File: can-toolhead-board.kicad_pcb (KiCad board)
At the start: 4 copper layers, 51 x 36.9 mm, 100 parts, among them J1 MF3-2x2P, J10 PH-2P, J11 PH-2P, J12 PH-2P, J13 PH-2P, J14 PH-2P, J15 PH-3P, J2 USB_C_Receptacle_USB2.0, J3 SH-6P, J4 PH-2P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

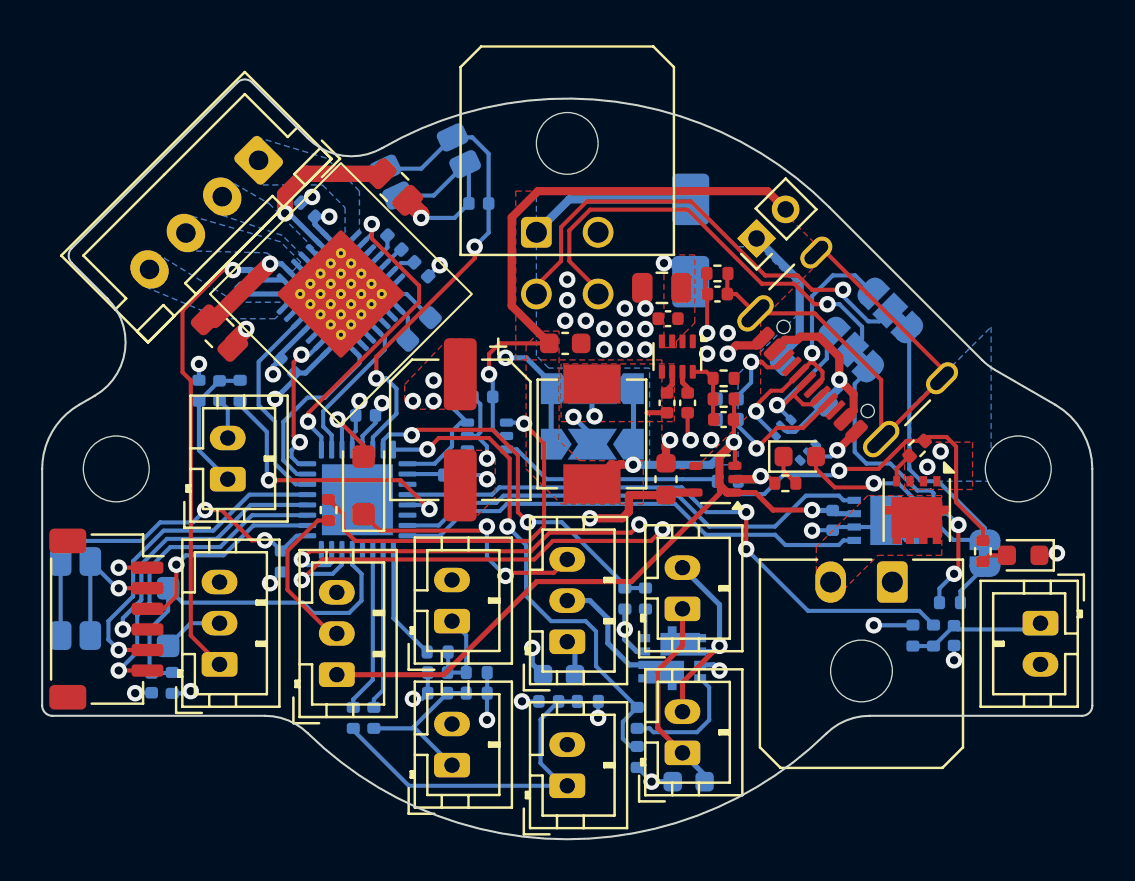
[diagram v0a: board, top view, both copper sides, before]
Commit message: Fixed up QFN pad routing and bypass cap vias
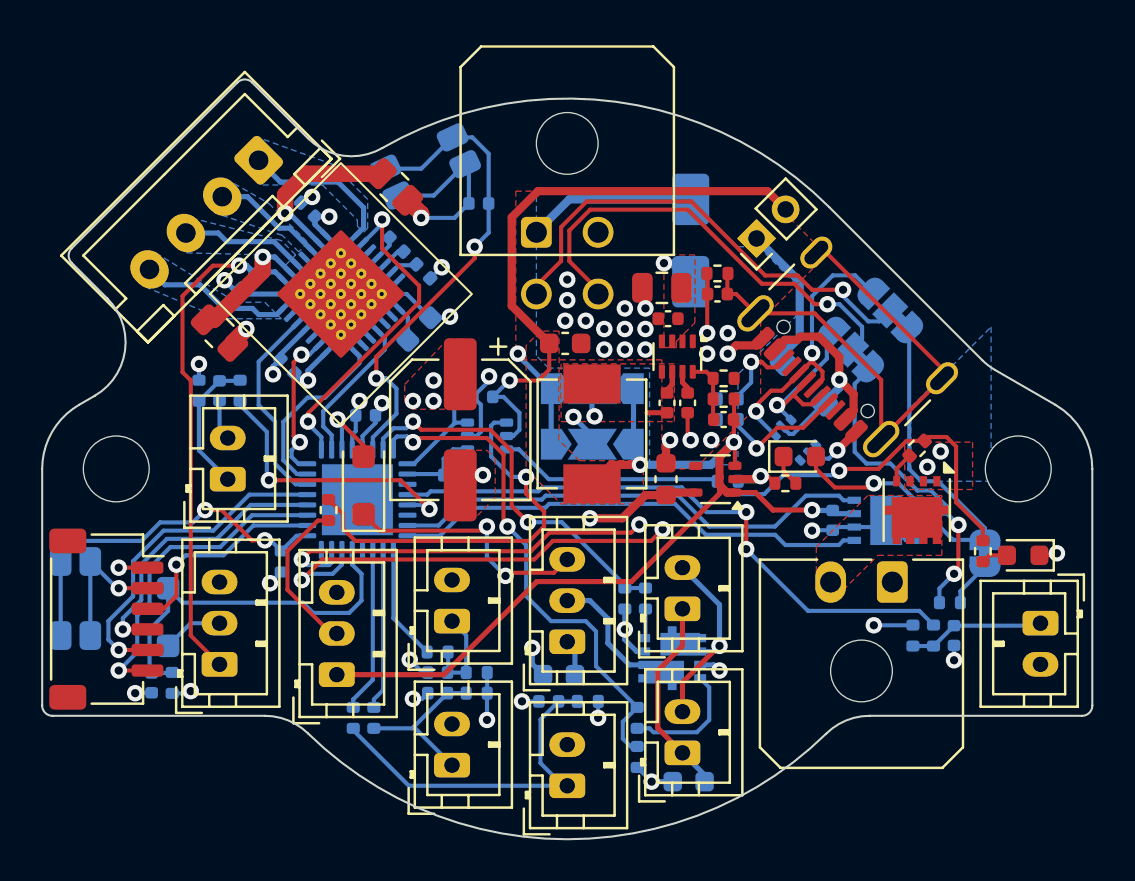
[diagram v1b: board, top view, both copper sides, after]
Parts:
- moved C16 0.14 mm to (93.0, 90.4)
- moved C17 0.14 mm to (91.7, 89.1)
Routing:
- net Net-(J9-Pin_1): track 0.00 -> 7.62 mm
- net Net-(J9-Pin_4): track 0.00 -> 7.54 mm
- net Net-(J9-Pin_3): track 0.00 -> 6.09 mm
- net Net-(J9-Pin_2): track 0.00 -> 5.47 mm
- net GND: track 75.8 -> 77.8 mm, vias 41 -> 44
- net +3V3: track 27.6 -> 26.0 mm
- net Net-(R17-Pad2): track 18.3 -> 19.2 mm
- net Net-(U6-BRA): track 5.41 -> 6.08 mm
- net RGB: track 5.67 -> 5.02 mm
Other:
- board text added: "${PCB_VERSION}"
- board text added: "UTB36"
- board text removed: "UTB36 ${PCB_VERSION}"

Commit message: Change input caps
- 100uF to electrolytic
- 10uF to 1206/50V
- Also fix LED on BOM to not be right angle lol
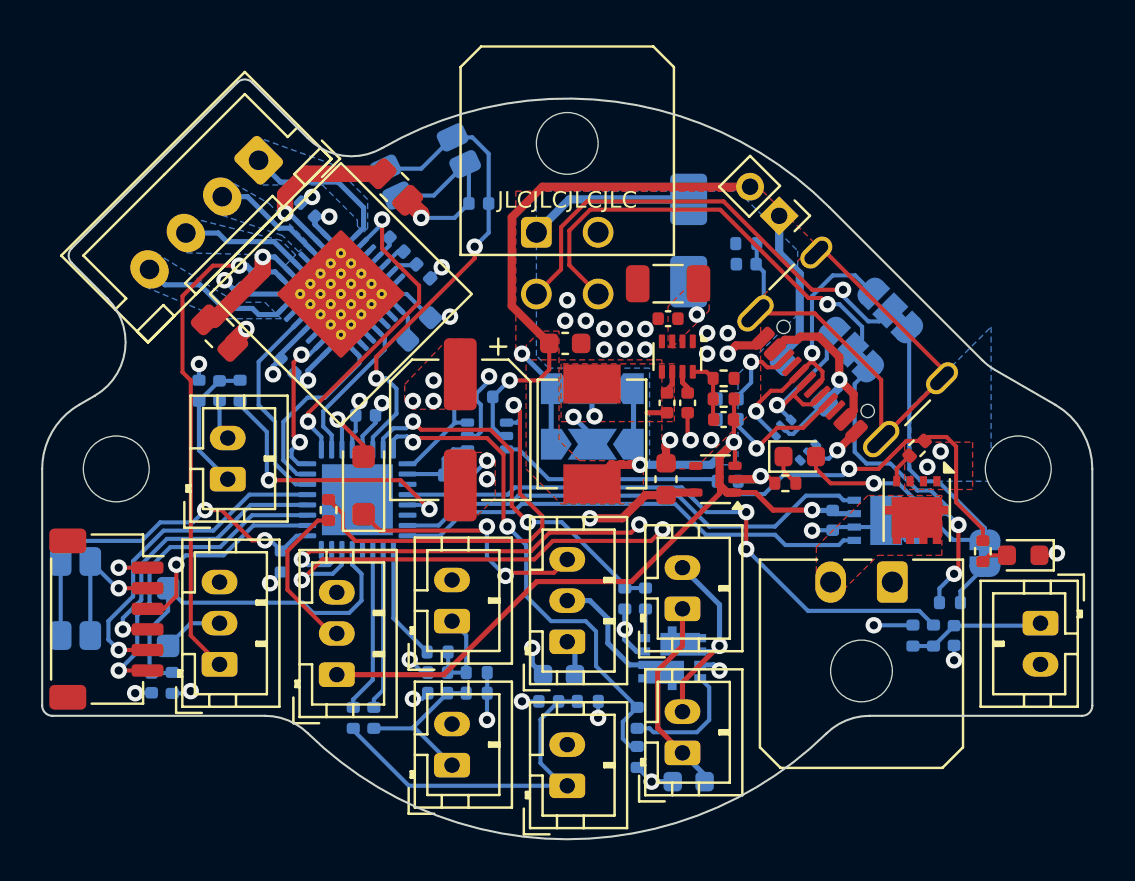
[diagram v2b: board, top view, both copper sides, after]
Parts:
- C2: value 10u/35V -> 10u/50V; footprint Capacitor_SMD:C_0805_2012Metric -> Capacitor_SMD:C_1206_3216Metric
- C9, R4: moved to B.Cu
- R18, R19: value 0R11 -> 0R11 1/3W
- R2: value 52K3 -> 52K3/1%
- R3: value 10K -> 10K/1%
- moved C9 2.02 mm to (108.7, 90.0)
- moved R4 2.02 mm to (108.7, 89.0)
- moved JP2 1.56 mm to (110.3, 87.7), turned to -135 degrees
- moved C2 0.36 mm to (104.9, 91.0)
- moved D1 0.10 mm to (105.9, 88.9)
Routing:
- net +5V: track 75.9 -> 73.0 mm
- net GND: track 77.8 -> 75.3 mm, vias 44 -> 42
- net Net-(J2-SHIELD): track 30.4 -> 31.3 mm
- net Net-(R17-Pad2): track 19.2 -> 20.0 mm
- net Net-(D2-K): track 7.21 -> 7.85 mm
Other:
- board text added: "JLCJLCJLCJLC"

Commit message: Change 5V out cap to 0805
- Shifted power/CAN connector a bit to make room, and added a bit of
  meat to the board around the mounting hole
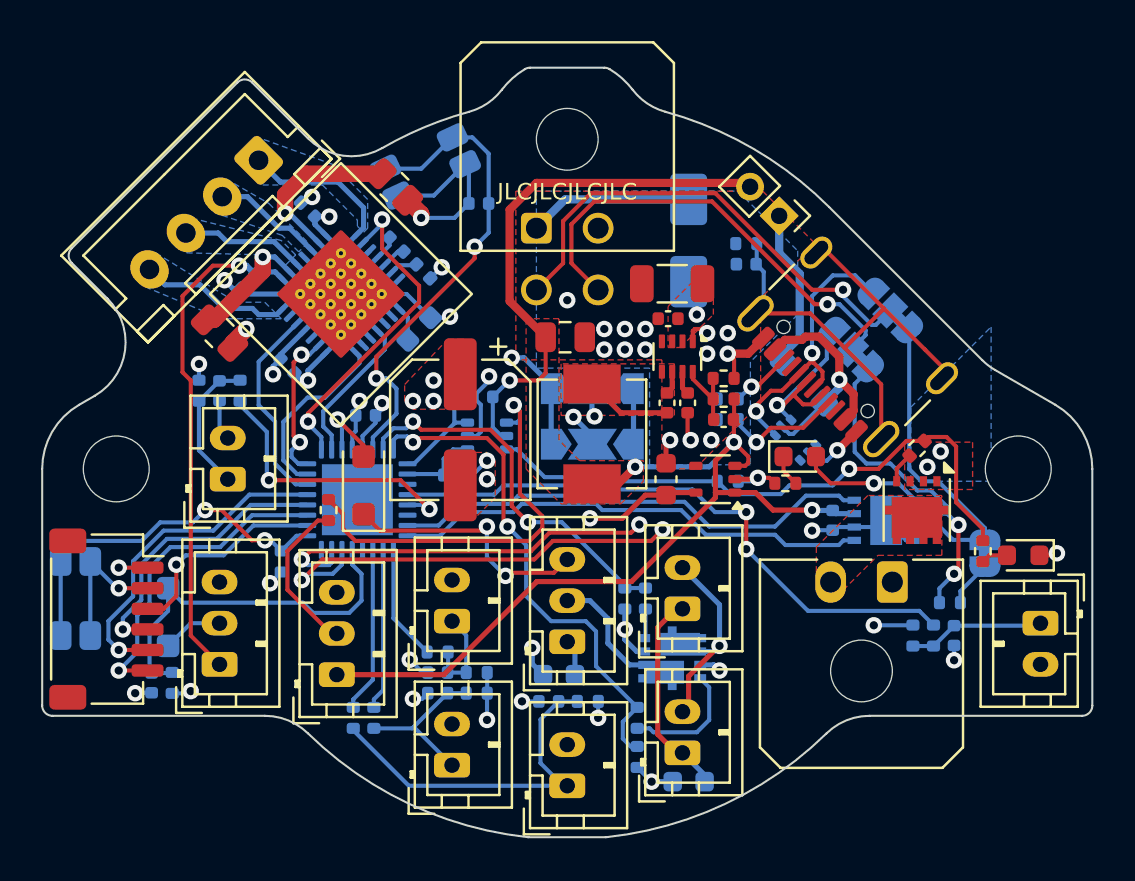
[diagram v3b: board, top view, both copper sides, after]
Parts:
- C1: value 100u/35V -> 100u
- C2: value 10u/50V -> 10u
- C7: value 22u/10V -> 22u; footprint Capacitor_SMD:C_0603_1608Metric -> Capacitor_SMD:C_0805_2012Metric
- moved C7 0.30 mm to (99.9, 93.6)
- moved J1 0.20 mm to (98.5, 88.3)
- moved C2 0.20 mm to (105.1, 91.0)
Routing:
- net Net-(J2-SHIELD): track 31.3 -> 25.6 mm
- net Net-(U1-SW): track 0.98 -> 4.23 mm
- net GND: track 75.3 -> 77.7 mm, vias 42 -> 40
- net +5V: track 73.0 -> 74.3 mm
- net Net-(J2-CC2): track 3.96 -> 3.05 mm
- net Net-(U1-FB): track 3.13 -> 3.75 mm
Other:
- board size 51 x 36.9 mm -> 51 x 37.4 mm

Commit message: Remove DNP from stuff where it doesn't belong in the schematic. Also DNP the fan port caps (the BOM ones weren't rated good for 24V anyway), but in any case since I couldn't find 4.7uF/35V/0603 good for 105C, reduce them to 2.2uF. Too bad I didn't make them 0805
Also added note for higher temp STM32, so I think all the components
should be good to 105C, except for the JST connectors...
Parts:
- C13, C14: value 4u7 -> 2u2

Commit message: Fix LCSC part for 74LVC2G17 (wrong package). List alternate parts in notes fields.
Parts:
- R18, R19: value 0R11 1/3W -> 0R11
- R22, R25: value 2K2 0.1% -> 2K2/0.1%
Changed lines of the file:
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@@
 			)
 		)
-		(property "Notes" ""
+		(property "Notes" "Alternates: Sumida 0530CDMCCDS-3R3MC"
 			(at 0 0 -90)
 			(unlocked yes)
@@
 			)
 		)
-		(property "Value" "0R11 1/3W"
+		(property "Value" "0R11"
 			(at 0 1.65 -45)
 			(layer "F.Fab")
@@
 			)
 		)
-		(property "Notes" ""
+		(property "Notes" "1/3 W"
 			(at 0 0 -45)
 			(unlocked yes)
@@
 			)
 		)
-		(property "manf#" "TLV70033DCKR"
+		(property "manf#" "MIC5365-3.3YC5-TR"
 			(at 0 0 180)
 			(unlocked yes)
@@
 			)
 		)
-		(property "Notes" ""
+		(property "Notes" "Alternates: TLV70033DCKx, AP2125KS-3.3TRG1"
 			(at 0 0 180)
 			(unlocked yes)
@@
 			)
 		)
-		(property "Notes" ""
+		(property "Notes" "Alternates: Amphenol 12402012E212A, GCT USB4105-GF-A, HRO TYPE-C-31-M-12, G-Switch GT-USB-7010ASV, XKB U263-16XN-4XS1735"
 			(at 0 0 135)
 			(unlocked yes)
@@
 			)
 		)
-		(property "LCSC" "C6837593;C5274553"
+		(property "LCSC" "C706997;C5274553"
 			(at 0 0 -135)
 			(unlocked yes)
@@
 			)
 		)
-		(property "Value" "0R11 1/3W"
+		(property "Value" "0R11"
 			(at 0 1.65 -45)
 			(layer "F.Fab")
@@
 			)
 		)
-		(property "Notes" ""
+		(property "Notes" "1/3 W"
 			(at 0 0 -45)
 			(unlocked yes)
@@
 			)
 		)
-		(property "Datasheet" ""
+		(property "Datasheet" "https://www.smc-diodes.com/propdf/DSS12U%20THRU%20DSS125U%20N1873%20REV.A.pdf"
 			(at 0 0 90)
 			(unlocked yes)
@@
 			)
 		)
-		(property "Datasheet" ""
+		(property "Datasheet" "https://www.smc-diodes.com/propdf/DSS12U%20THRU%20DSS125U%20N1873%20REV.A.pdf"
 			(at 0 0 -90)
 			(unlocked yes)
@@
 			)
 		)
-		(property "LCSC" "C7394037"
+		(property "LCSC" "C7394022"
 			(at 0 0 0)
 			(unlocked yes)
@@
 			)
 		)
-		(property "Value" "2K2 0.1%"
+		(property "Value" "2K2/0.1%"
 			(at 0 -1.17 90)
 			(layer "B.Fab")
@@
 			)
 		)
-		(property "Notes" ""
+		(property "Notes" "Use STM32G0B1KxU7 for 105C temperature rating"
 			(at 0 0 -90)
 			(unlocked yes)
@@
 			)
 		)
-		(property "Datasheet" ""
+		(property "Datasheet" "https://www.smc-diodes.com/propdf/DSS12U%20THRU%20DSS125U%20N1873%20REV.A.pdf"
 			(at 0 0 135)
 			(unlocked yes)
@@
 			)
 		)
-		(property "Value" "2K2 0.1%"
+		(property "Value" "2K2/0.1%"
 			(at 0 -1.17 90)
 			(layer "B.Fab")
@@
 			)
 		)
-		(property "Datasheet" ""
+		(property "Datasheet" "https://diotec.com/request/datasheet/sk34sma-3g.pdf"
 			(at 0 0 -90)
 			(unlocked yes)
